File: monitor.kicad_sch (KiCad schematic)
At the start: 43 parts, among them J1 A, J2 B, J3 Abuf, J4 Bbuf, J5 Sum, J6 Gnd, U704 OPA2197D, U76 OPA2189DGK, U77 OPA2388DGK, U78 OPA2189DGK

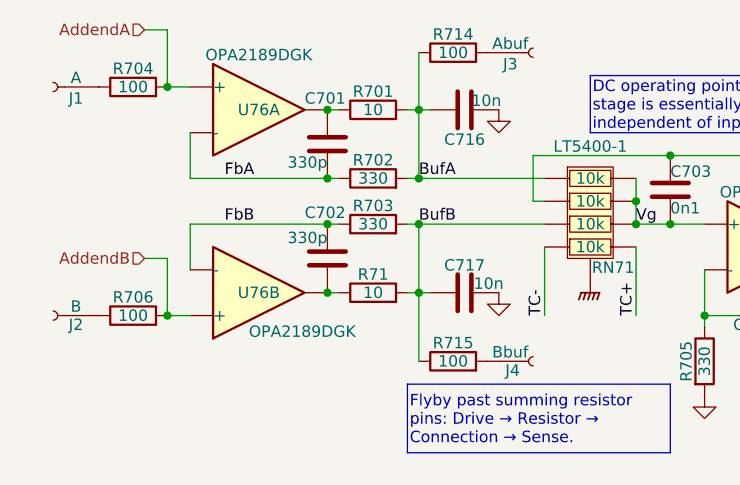
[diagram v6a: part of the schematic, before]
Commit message: Simplify relay drive.
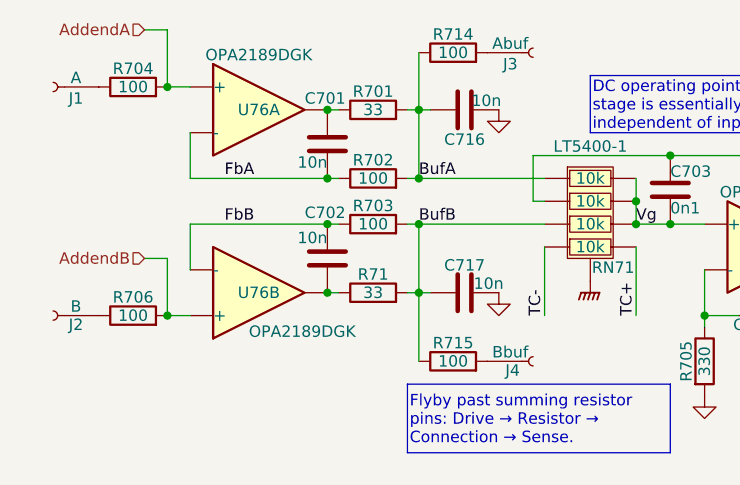
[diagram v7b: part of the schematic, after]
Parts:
- C701, C702: value 330p -> 10n; LCSC C1664 -> C307500
- R701, R71: value 10 -> 33; LCSC C25077 -> C25105
- R702, R703: value 330 -> 100; LCSC C25104 -> C25076
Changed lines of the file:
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@@
 			)
 		)
-		(property "Value" "10"
+		(property "Value" "33"
 			(at 114.3 92.71 90)
 			(effects
@@
 			)
 		)
-		(property "LCSC" "C25077"
+		(property "LCSC" "C25105"
 			(at 114.3 92.71 90)
 			(effects
@@
 			)
 		)
-		(property "Value" "330p"
+		(property "Value" "10n"
 			(at 109.22 78.232 0)
 			(effects
@@
 			)
 		)
-		(property "Datasheet" "C0G, 50V"
+		(property "Datasheet" "C0G, 25V"
 			(at 109.22 76.2 0)
 			(effects
@@
 			)
 		)
-		(property "LCSC" "C1664"
+		(property "LCSC" "C307500"
 			(at 109.22 76.2 0)
 			(effects
@@
 			)
 		)
-		(property "Value" "330"
+		(property "Value" "100"
 			(at 114.3 80.01 90)
 			(effects
@@
 			)
 		)
-		(property "LCSC" "C25104"
+		(property "LCSC" "C25076"
 			(at 114.3 80.01 90)
 			(effects
@@
 			)
 		)
-		(property "Value" "330"
+		(property "Value" "100"
 			(at 114.3 85.09 90)
 			(effects
@@
 			)
 		)
-		(property "LCSC" "C25104"
+		(property "LCSC" "C25076"
 			(at 114.3 85.09 90)
 			(effects
@@
 			)
 		)
-		(property "Value" "10"
+		(property "Value" "33"
 			(at 114.3 72.39 90)
 			(effects
@@
 			)
 		)
-		(property "LCSC" "C25077"
+		(property "LCSC" "C25105"
 			(at 114.3 72.39 90)
 			(effects
@@
 			)
 		)
-		(property "Value" "330p"
+		(property "Value" "10n"
 			(at 109.22 86.614 0)
 			(effects
@@
 			)
 		)
-		(property "Datasheet" "C0G, 50V"
+		(property "Datasheet" "C0G, 25V"
 			(at 109.22 88.9 0)
 			(effects
@@
 			)
 		)
-		(property "LCSC" "C1664"
+		(property "LCSC" "C307500"
 			(at 109.22 88.9 0)
 			(effects

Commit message: Tweak various feedback loops.
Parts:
- U77: Stock 14 -> 14+LCSC
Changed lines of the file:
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@@
 			)
 		)
-		(property "Sim.Library" "spice/opa2388.lib"
-			(at 158.75 87.63 0)
-			(effects
-				(font
-					(size 1.27 1.27)
-				)
-				(hide yes)
-			)
-		)
-		(property "Sim.Name" "OPA2388"
-			(at 158.75 87.63 0)
-			(effects
-				(font
-					(size 1.27 1.27)
-				)
-				(hide yes)
-			)
-		)
-		(property "Sim.Device" "SUBCKT"
-			(at 158.75 87.63 0)
-			(effects
-				(font
-					(size 1.27 1.27)
-				)
-				(hide yes)
-			)
-		)
-		(property "Sim.Pins" "1=aout 2=a- 3=a+ 4=v- 5=b+ 6=b- 7=bout 8=v+"
-			(at 158.75 87.63 0)
-			(effects
-				(font
-					(size 1.27 1.27)
-				)
-				(hide yes)
-			)
-		)
-		(property "Stock" "14"
+		(property "Stock" "14+LCSC"
 			(at 158.75 87.63 0)
 			(effects
@@
 			)
 		)
-		(property "Sim.Library" "spice/opa2388.lib"
-			(at 208.28 135.89 0)
-			(effects
-				(font
-					(size 1.27 1.27)
-				)
-				(hide yes)
-			)
-		)
-		(property "Sim.Name" "OPA2388"
-			(at 208.28 135.89 0)
-			(effects
-				(font
-					(size 1.27 1.27)
-				)
-				(hide yes)
-			)
-		)
-		(property "Sim.Device" "SUBCKT"
-			(at 208.28 135.89 0)
-			(effects
-				(font
-					(size 1.27 1.27)
-				)
-				(hide yes)
-			)
-		)
-		(property "Sim.Pins" "1=aout 2=a- 3=a+ 4=v- 5=b+ 6=b- 7=bout 8=v+"
-			(at 208.28 135.89 0)
-			(effects
-				(font
-					(size 1.27 1.27)
-				)
-				(hide yes)
-			)
-		)
-		(property "Stock" "14"
+		(property "Stock" "14+LCSC"
 			(at 208.28 135.89 0)
 			(effects
@@
 			)
 		)
-		(property "Sim.Library" "spice/opa2388.lib"
+		(property "Stock" "14+LCSC"
 			(at 209.55 106.68 0)
 			(effects
-				(font
-					(size 1.27 1.27)
-				)
-				(hide yes)
-			)
-		)
-		(property "Sim.Name" "OPA2388"
-			(at 209.55 106.68 0)
-			(effects
-				(font
-					(size 1.27 1.27)
-				)
-				(hide yes)
-			)
-		)
-		(property "Sim.Device" "SUBCKT"
-			(at 209.55 106.68 0)
-			(effects
-				(font
-					(size 1.27 1.27)
-				)
-				(hide yes)
-			)
-		)
-		(property "Sim.Pins" "1=aout 2=a- 3=a+ 4=v- 5=b+ 6=b- 7=bout 8=v+"
-			(at 209.55 106.68 0)
-			(effects
-				(font
-					(size 1.27 1.27)
-				)
-				(hide yes)
-			)
-		)
-		(property "Stock" "14"
-			(at 209.55 106.68 0)
-			(effects
